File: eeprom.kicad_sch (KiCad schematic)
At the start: 8 parts, among them U2 AT24C04C_SOIC8

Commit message: [#93514] Propagate title and date across all of the sheets
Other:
- title: (none) -> Datacenter Secure Control Module Breakout Board
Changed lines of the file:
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@@
 	(generator_version "9.0")
 	(paper "A3")
+	(title_block
+		(title "Datacenter Secure Control Module Breakout Board")
+		(date "2021-12-16")
+		(rev "2.0.0")
+	)
 	(text "LEDs + TPs"
 		(exclude_from_sim no)

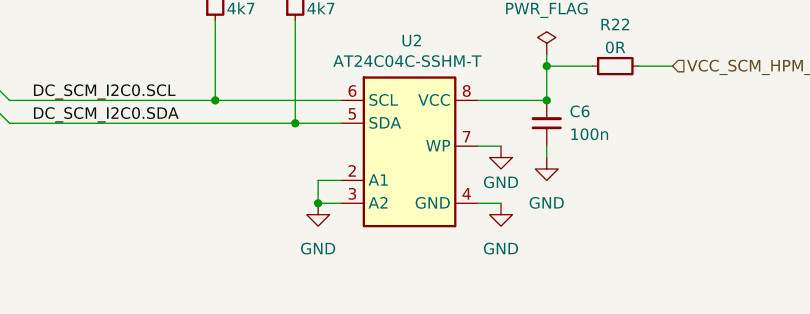
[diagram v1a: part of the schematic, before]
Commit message: [#93514] Add address note to EEPROM
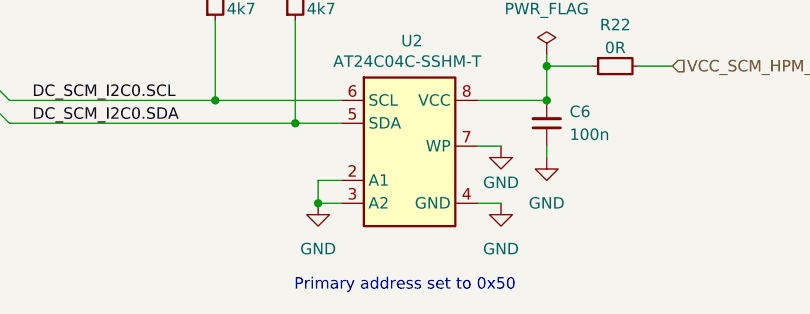
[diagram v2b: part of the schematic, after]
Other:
- note added: "Primary address set to 0x50"
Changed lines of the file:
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@@
+		)
+	)
+	(text "Primary address set to 0x50"
+		(exclude_from_sim no)
+		(at 92.202 87.884 0)
+		(effects
+			(font
+				(size 1.27 1.27)
+			)
 		)
 	)
